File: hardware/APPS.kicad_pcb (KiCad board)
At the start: 2 copper layers, 100 x 75 mm, 102 parts, among them J1 Signals, J2 Diagnostics, J3 Power & CAN, K1 FINDER-30.22, Q1 BSS138, SW1 SW_Push, U1 STM32L4P5RET6, U2 MCP6N11-005, U3 MCP6N11-005, U4 MCP6001, U5 MCP6001, U6 MCP2562-H-SN, U7 LM1117-3.3, U8 LM1117-3.3, U9 LM1117-3.3, Y1 8Mhz

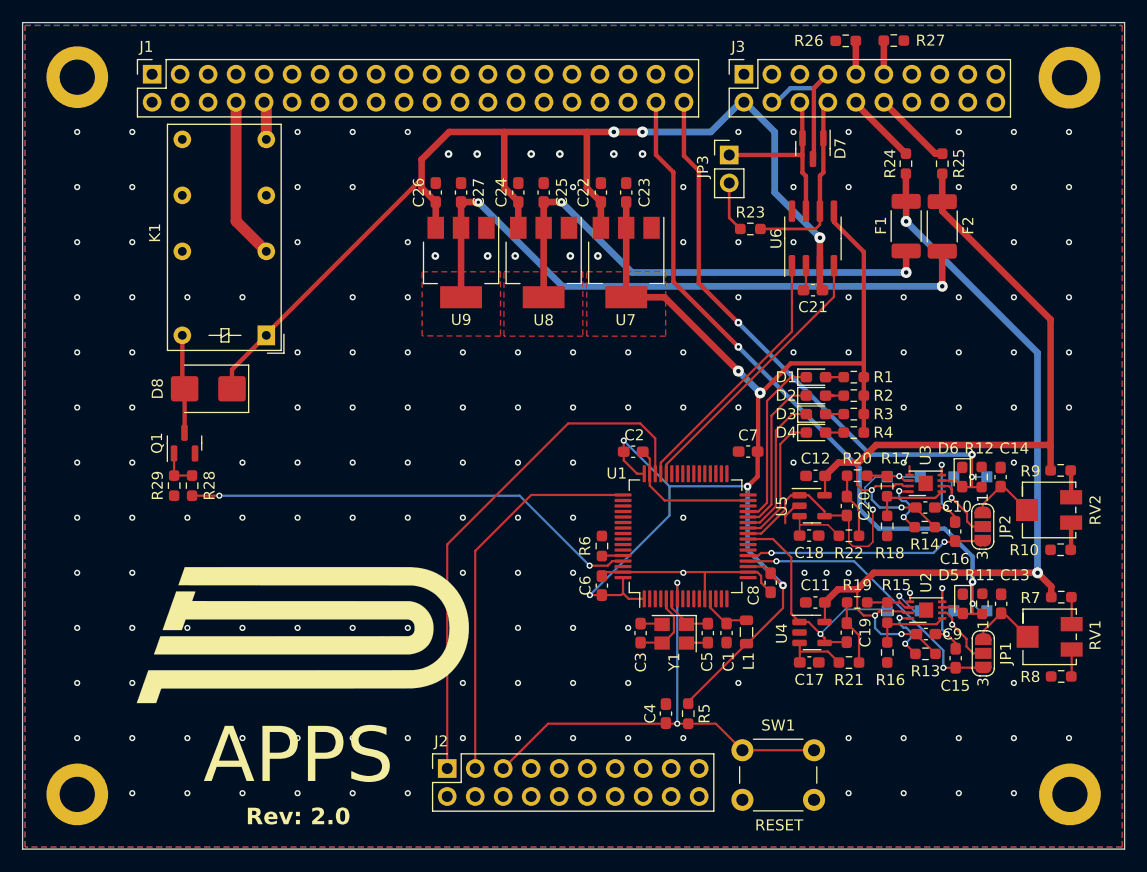
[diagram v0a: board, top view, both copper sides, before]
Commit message: Add brake pressure sensors
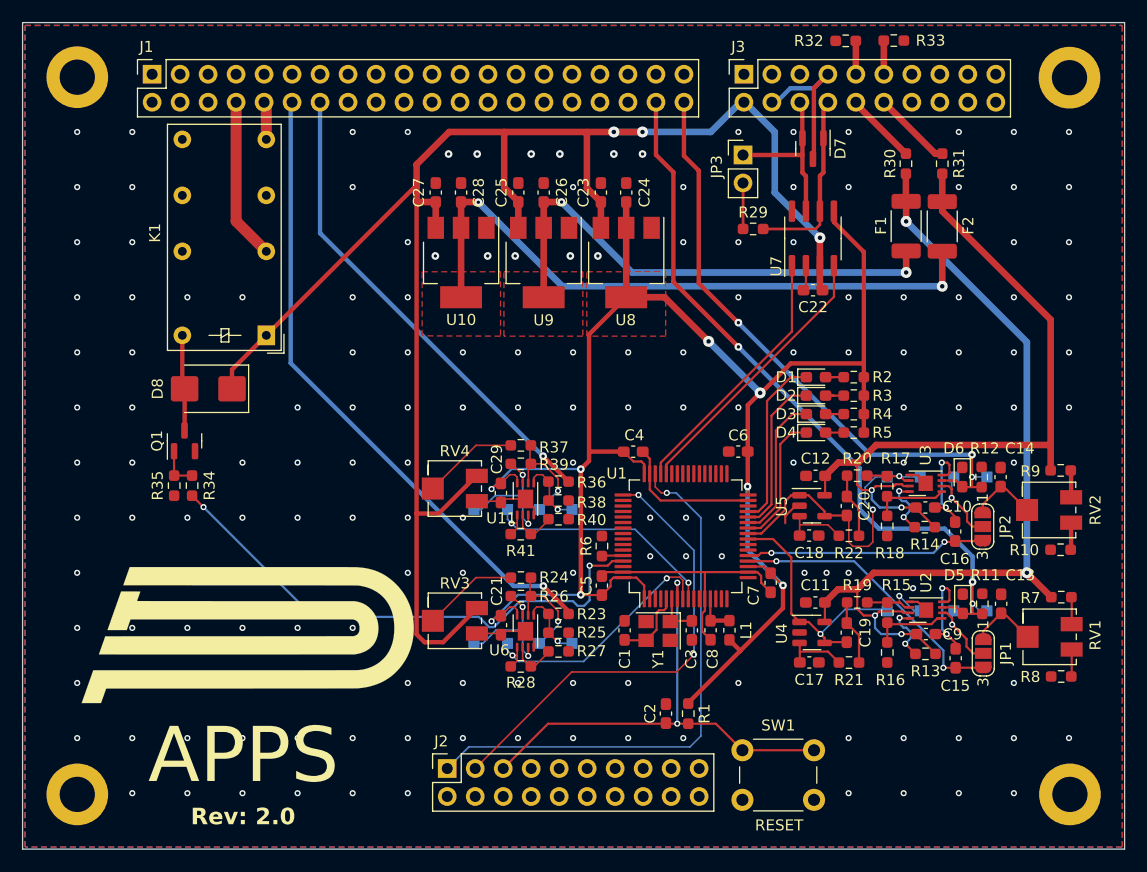
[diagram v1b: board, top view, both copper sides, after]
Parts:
- added C21: 100n, Capacitor_SMD:C_0603_1608Metric_Pad1.08x0.95mm_HandSolder, F.Cu at (142.5, 120.8)
- added C29: 100n, Capacitor_SMD:C_0603_1608Metric_Pad1.08x0.95mm_HandSolder, F.Cu at (142.4, 108.8)
- added R23: 1k, Resistor_SMD:R_0603_1608Metric_Pad0.98x0.95mm_HandSolder, F.Cu at (147.7, 119.7)
- added R24: 10k, Resistor_SMD:R_0603_1608Metric_Pad0.98x0.95mm_HandSolder, F.Cu at (144.3, 116.4)
- added R25: 2k, Resistor_SMD:R_0603_1608Metric_Pad0.98x0.95mm_HandSolder, F.Cu at (147.7, 121.4)
- added R26: 2k, Resistor_SMD:R_0603_1608Metric_Pad0.98x0.95mm_HandSolder, F.Cu at (144.3, 118.1)
- added R27: TBD, Resistor_SMD:R_0603_1608Metric_Pad0.98x0.95mm_HandSolder, F.Cu at (147.7, 123.1)
- added R28: TBD, Resistor_SMD:R_0603_1608Metric_Pad0.98x0.95mm_HandSolder, F.Cu at (144.3, 124.5)
- added R36: 1k, Resistor_SMD:R_0603_1608Metric_Pad0.98x0.95mm_HandSolder, F.Cu at (147.7, 107.7)
- added R37: 10k, Resistor_SMD:R_0603_1608Metric_Pad0.98x0.95mm_HandSolder, F.Cu at (144.3, 104.4)
- added R38: 2k, Resistor_SMD:R_0603_1608Metric_Pad0.98x0.95mm_HandSolder, F.Cu at (147.7, 109.4)
- added R39: 2k, Resistor_SMD:R_0603_1608Metric_Pad0.98x0.95mm_HandSolder, F.Cu at (144.3, 106.1)
- added R40: TBD, Resistor_SMD:R_0603_1608Metric_Pad0.98x0.95mm_HandSolder, F.Cu at (147.7, 111.1)
- added R41: TBD, Resistor_SMD:R_0603_1608Metric_Pad0.98x0.95mm_HandSolder, F.Cu at (144.2, 112.5)
- added RV3: 2k, Potentiometer_SMD:Potentiometer_Bourns_3214J_Horizontal, F.Cu at (138.3, 120.4)
- added RV4: 2k, Potentiometer_SMD:Potentiometer_Bourns_3214J_Horizontal, F.Cu at (138.3, 108.4)
- added TP10: ~, TestPoint:TestPoint_Pad_1.0x1.0mm, B.Cu at (145.9, 122.4)
- added TP11: ~, TestPoint:TestPoint_Pad_1.0x1.0mm, B.Cu at (140.0, 122.4)
- added TP12: OUT, TestPoint:TestPoint_Pad_1.0x1.0mm, B.Cu at (143.1, 122.4)
- added TP13: ~, TestPoint:TestPoint_Pad_1.0x1.0mm, B.Cu at (148.9, 110.3)
- added TP14: ~, TestPoint:TestPoint_Pad_1.0x1.0mm, B.Cu at (145.9, 110.3)
- added TP15: ~, TestPoint:TestPoint_Pad_1.0x1.0mm, B.Cu at (140.0, 110.3)
- added TP16: OUT, TestPoint:TestPoint_Pad_1.0x1.0mm, B.Cu at (143.1, 110.3)
- added TP9: ~, TestPoint:TestPoint_Pad_1.0x1.0mm, B.Cu at (148.9, 122.4)
- added U11: MCP6002-xMC, Package_DFN_QFN:DFN-8-1EP_3x2mm_P0.5mm_EP1.7x1.4mm, F.Cu at (144.7, 109.3)
- added U6: MCP6002-xMC, Package_DFN_QFN:DFN-8-1EP_3x2mm_P0.5mm_EP1.7x1.4mm, F.Cu at (144.7, 121.3)
- L1: footprint Inductor_SMD:L_0805_2012Metric -> Inductor_SMD:L_0603_1608Metric_Pad1.05x0.95mm_HandSolder
- moved G*** 10.0 mm to (149.2, 93.4)
- moved G*** 5.00 mm to (118.6, 121.3)
- moved L1 1.56 mm to (163.2, 121.2)
- moved C8 1.47 mm to (161.5, 121.2)
- moved Y1 1.47 mm to (156.7, 121.3)
- moved C1 1.47 mm to (153.7, 121.2)
- moved C3 1.47 mm to (159.8, 121.2)
- moved JP3 1.25 mm to (164.4, 78.1)
- moved C6 0.90 mm to (164.0, 105.0)
- moved R29 0.25 mm to (165.3, 84.8)
- moved Q1 0.20 mm to (113.7, 104.0)
- renumbered C3 to C1, C4 to C2, C21 to C22, C22 to C23, C23 to C24, C24 to C25, C25 to C26, C26 to C27, C27 to C28, C5 to C3, C2 to C4, C6 to C5, C7 to C6, C8 to C7, C1 to C8, R5 to R1, R1 to R2, R23 to R29, R2 to R3, R24 to R30, R25 to R31, R26 to R32, R27 to R33, R28 to R34, R29 to R35, R3 to R4, R4 to R5, TP5 to TP3, TP6 to TP4, TP3 to TP5, TP7 to TP6, TP4 to TP7, U9 to U10, U6 to U7, U7 to U8, U8 to U9
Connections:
- net /Power Module/VO_POT1 renamed /Power/VO_POT1
- net /Power Module/VO_POT2 renamed /Power/VO_POT2
- J1 pad 12: unconnected-(J1-Pin_12-Pad12) -> BRK_PRESS_LEFT
- J1 pad 14: unconnected-(J1-Pin_14-Pad14) -> BRK_PRESS_RIGHT
- U1 pad 8: unconnected-(U1-PC0-Pad8) -> /BRAKE_PRESSURE1
- U1 pad 9: unconnected-(U1-PC1-Pad9) -> /BRAKE_PRESSURE2
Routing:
- net BRK_PRESS_LEFT: track 0.00 -> 58.5 mm, vias 0 -> 1
- net +5V: track 105.4 -> 159.3 mm
- net BRK_PRESS_RIGHT: track 0.00 -> 43.8 mm, vias 0 -> 1
- net /3V3_SYS: track 131.8 -> 164.8 mm, vias 6 -> 8
- net /BRAKE_PRESSURE1: track 0.00 -> 24.3 mm, vias 0 -> 2
- net /BRAKE_PRESSURE2: track 0.00 -> 23.6 mm, vias 0 -> 2
- net GND: track 72.2 -> 89.9 mm, vias 178 -> 169
- net Net-(U11A-+): track 0.00 -> 12.5 mm, vias 0 -> 2
- net Net-(U6A-+): track 0.00 -> 12.5 mm, vias 0 -> 2
- net Net-(U6B--): track 0.00 -> 10.2 mm, vias 0 -> 1
- net Net-(U11B--): track 0.00 -> 9.99 mm, vias 0 -> 1
- net Net-(R37-Pad2): track 0.00 -> 8.79 mm
- net Net-(R24-Pad2): track 0.00 -> 8.79 mm
- net /EN_RELAY: track 42.0 -> 48.8 mm
- net CLK: track 35.3 -> 42.1 mm, vias 0 -> 2
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
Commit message: Add 0R resistors to the brake pressure signals
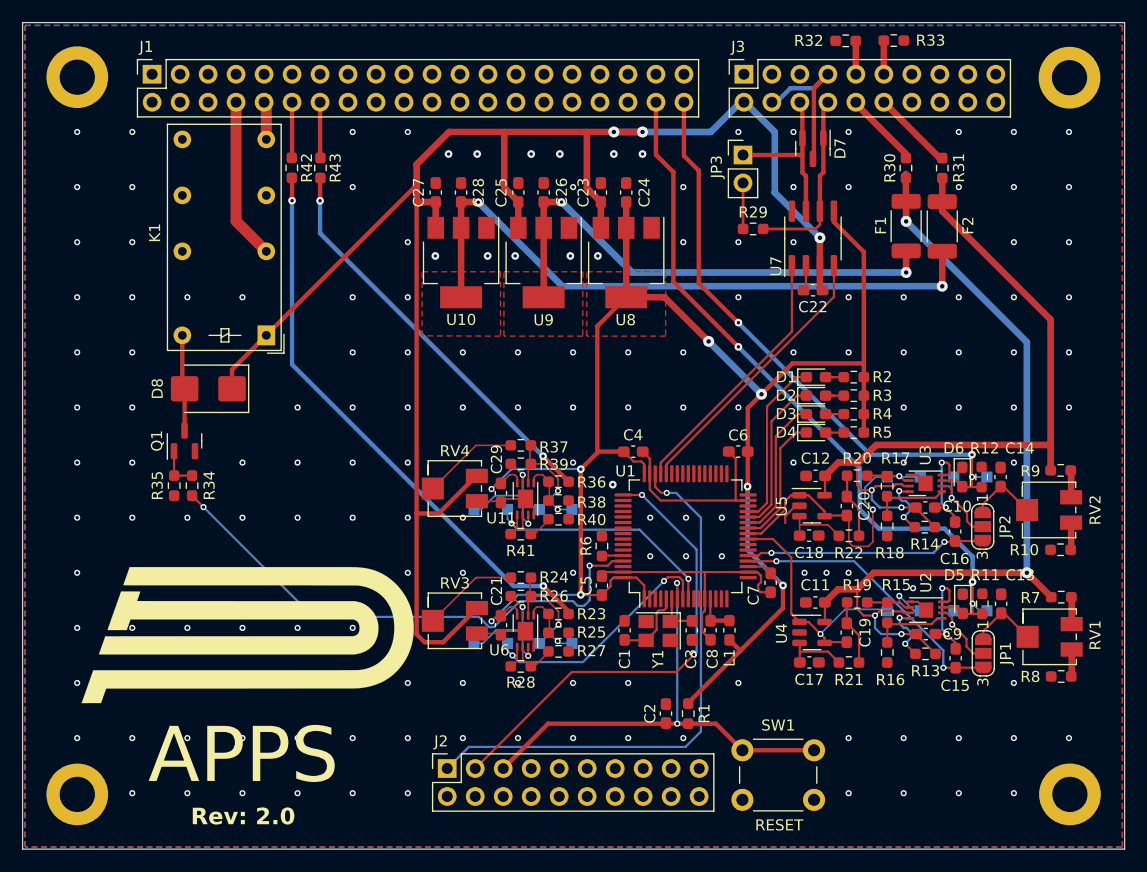
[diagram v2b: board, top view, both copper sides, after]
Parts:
- added R42: 0R, Resistor_SMD:R_0603_1608Metric_Pad0.98x0.95mm_HandSolder, F.Cu at (123.5, 79.3)
- added R43: 0R, Resistor_SMD:R_0603_1608Metric_Pad0.98x0.95mm_HandSolder, F.Cu at (126.1, 79.3)
- moved R31 0.40 mm to (182.5, 79.3)
- moved R30 0.40 mm to (179.2, 79.3)
- moved G*** 0.28 mm to (149.0, 93.6)
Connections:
- D1 pad 1: /LED4 -> /LED1
- D2 pad 1: /LED3 -> /LED2
- D3 pad 1: /LED2 -> /LED3
- D4 pad 1: /LED1 -> /LED4
- J1 pad 12: BRK_PRESS_LEFT -> Net-(J1-Pin_12)
- J1 pad 14: BRK_PRESS_RIGHT -> Net-(J1-Pin_14)
- U1 pad 26: /LED1 -> /LED4
- U1 pad 27: /LED2 -> /LED3
- U1 pad 28: /LED3 -> /LED2
- U1 pad 29: /LED4 -> /LED1
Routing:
- net BRK_PRESS_LEFT: track 58.5 -> 51.6 mm, vias 1 -> 2
- net BRK_PRESS_RIGHT: track 43.8 -> 36.9 mm, vias 1 -> 2
- net GND: track 89.9 -> 95.6 mm, vias 169 -> 170
- net Net-(J1-Pin_14): track 0.00 -> 5.07 mm
- net Net-(J1-Pin_12): track 0.00 -> 5.05 mm
- net /LED4: track 15.8 -> 12.1 mm
- net /LED1: track 12.3 -> 15.5 mm
- net /LED3: track 14.6 -> 13.1 mm
- net /LED2: track 13.4 -> 14.3 mm
- net /3V3_SYS: track 164.8 -> 164.1 mm

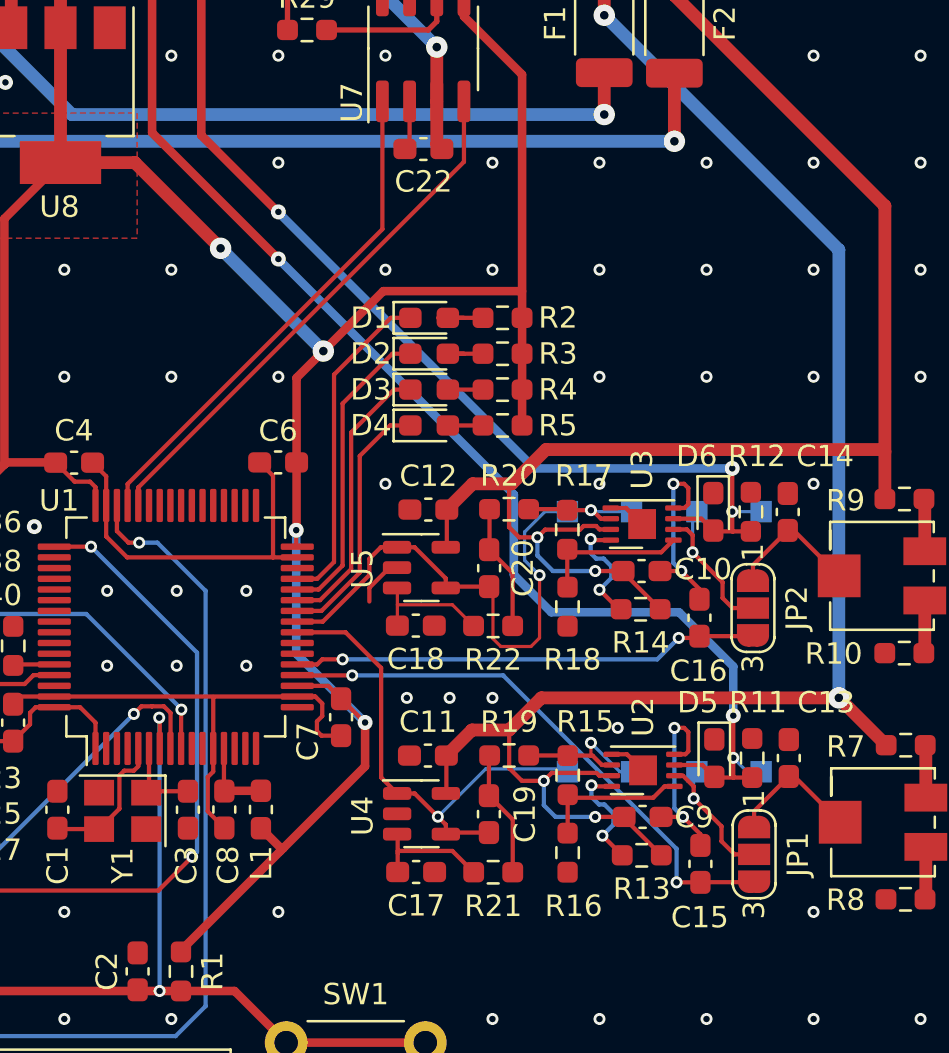
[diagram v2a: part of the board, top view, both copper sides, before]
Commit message: Use bridged solder jumpers
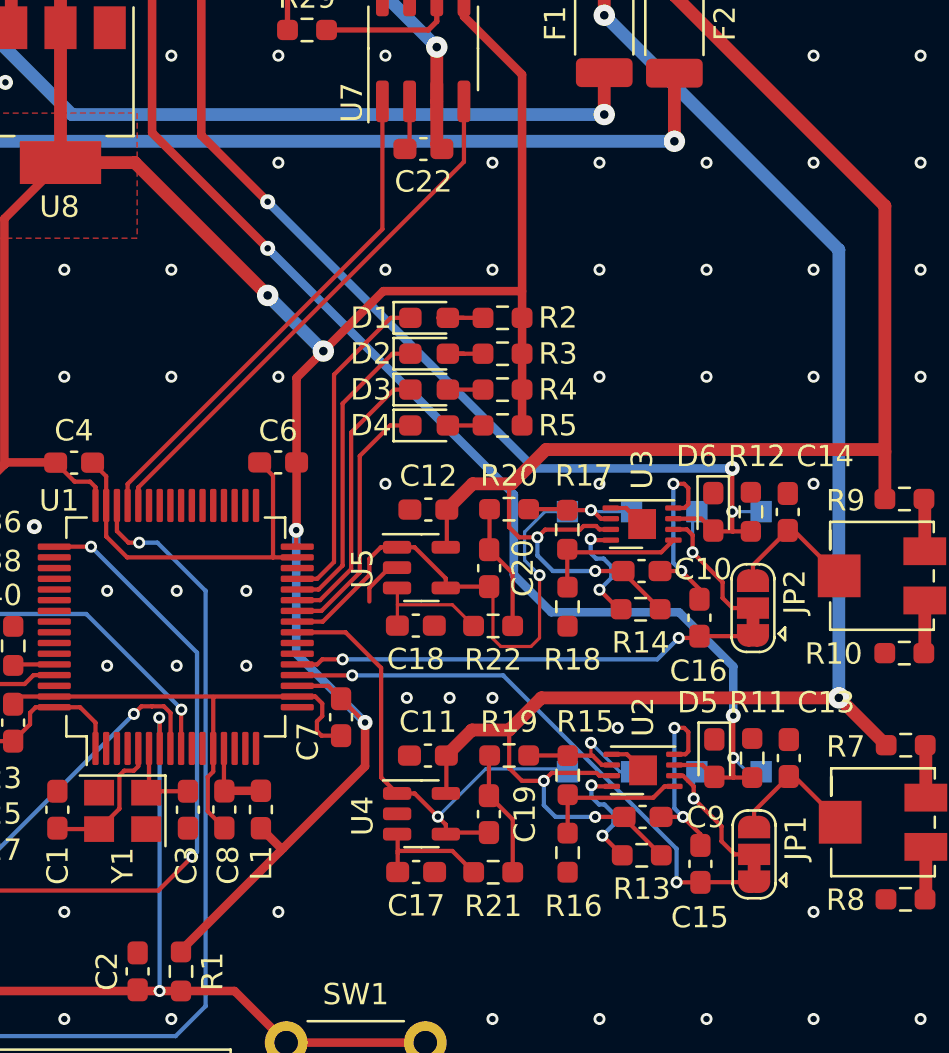
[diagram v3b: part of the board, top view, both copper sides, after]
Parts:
- JP1, JP2: footprint Jumper:SolderJumper-3_P1.3mm_Open_RoundedPad1.0x1.5mm_NumberLabels -> Jumper:SolderJumper-3_P1.3mm_Bridged12_RoundedPad1.0x1.5mm
- turned JP1 to 90 degrees
- turned JP2 to 90 degrees
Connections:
- C13 pad 1: Net-(JP1-A) -> Net-(JP1-B)
- C14 pad 1: Net-(JP2-A) -> Net-(JP2-B)
- JP1 pad 1: Net-(JP1-A) -> /DAC_REF1
- JP1 pad 3: /DAC_REF1 -> Net-(JP1-B)
- JP2 pad 1: Net-(JP2-A) -> /DAC_REF2
- JP2 pad 3: /DAC_REF2 -> Net-(JP2-B)
- RV1 pad 2: Net-(JP1-A) -> Net-(JP1-B)
- RV2 pad 2: Net-(JP2-A) -> Net-(JP2-B)
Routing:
- net Net-(JP1-B): track 0.00 -> 6.29 mm
- net Net-(JP1-A): track 6.29 -> 0.00 mm
- net Net-(JP2-B): track 0.00 -> 6.28 mm
- net Net-(JP2-A): track 6.28 -> 0.00 mm

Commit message: Change test points footprints
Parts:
- TP1: value P1 -> APPS_P; footprint TestPoint:TestPoint_Pad_1.0x1.0mm -> TestPoint:TestPoint_Pad_D1.0mm
- TP10, TP14: value ~ -> BR_N; footprint TestPoint:TestPoint_Pad_1.0x1.0mm -> TestPoint:TestPoint_Pad_D1.0mm
- TP11, TP15: value ~ -> BR_MID; footprint TestPoint:TestPoint_Pad_1.0x1.0mm -> TestPoint:TestPoint_Pad_D1.0mm
- TP12, TP16: value OUT -> BR_OUT; footprint TestPoint:TestPoint_Pad_1.0x1.0mm -> TestPoint:TestPoint_Pad_D1.0mm
- TP13, TP9: value ~ -> BR_P; footprint TestPoint:TestPoint_Pad_1.0x1.0mm -> TestPoint:TestPoint_Pad_D1.0mm
- TP2: value N1 -> APPS_N; footprint TestPoint:TestPoint_Pad_1.0x1.0mm -> TestPoint:TestPoint_Pad_D1.0mm
- TP3: value P2 -> APPS_P; footprint TestPoint:TestPoint_Pad_1.0x1.0mm -> TestPoint:TestPoint_Pad_D1.0mm
- TP4: value N2 -> APPS_N; footprint TestPoint:TestPoint_Pad_1.0x1.0mm -> TestPoint:TestPoint_Pad_D1.0mm
- TP5: value O1 -> APPS_MID; footprint TestPoint:TestPoint_Pad_1.0x1.0mm -> TestPoint:TestPoint_Pad_D1.0mm
- TP6: value O2 -> APPS_MID; footprint TestPoint:TestPoint_Pad_1.0x1.0mm -> TestPoint:TestPoint_Pad_D1.0mm
- TP7: value F1 -> APPS_OUT; footprint TestPoint:TestPoint_Pad_1.0x1.0mm -> TestPoint:TestPoint_Pad_D1.0mm
- TP8: value F2 -> APPS_OUT; footprint TestPoint:TestPoint_Pad_1.0x1.0mm -> TestPoint:TestPoint_Pad_D1.0mm
